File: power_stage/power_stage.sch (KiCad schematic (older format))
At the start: 18 parts, among them J1 Conn_02x12_Odd_Even, U1 ISO7321C, U2 XMC1301T016F0032ABXUMA1, U3 LP2951, X1 PDS1-S5-S15-M-TR

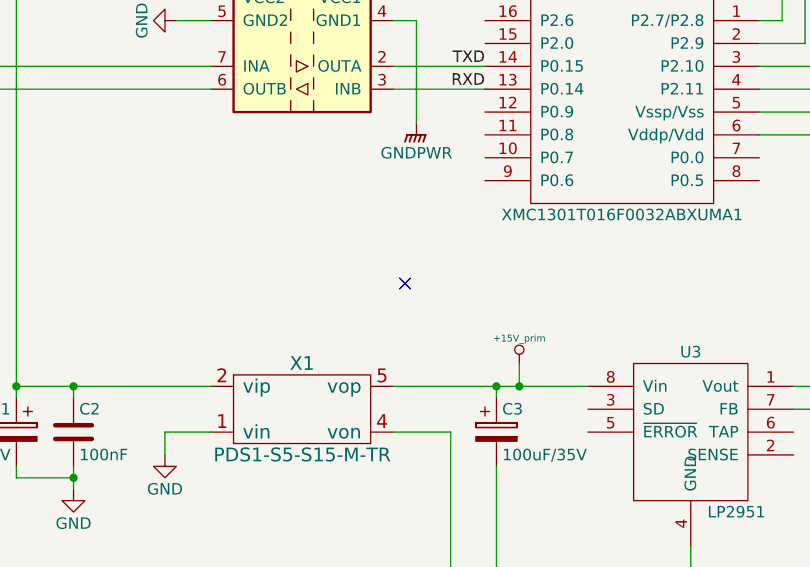
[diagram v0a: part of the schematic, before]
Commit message: Starting the control_stage (copied from small_drive)
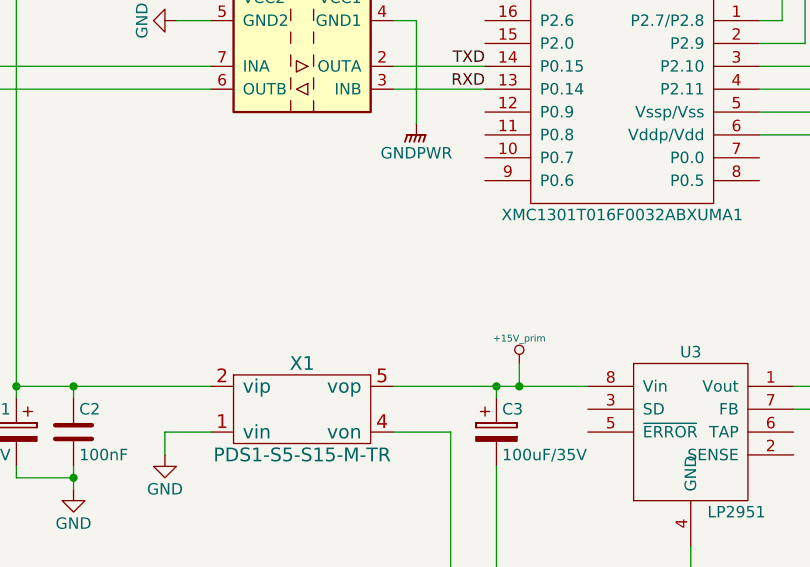
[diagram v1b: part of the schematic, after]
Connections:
- no-connect marks 1 -> 0
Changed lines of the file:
@@
 Wire Wire Line
 	5050 3650 5050 3600
-NoConn ~ 5000 4900
 Wire Wire Line
 	2050 2150 2050 2100
